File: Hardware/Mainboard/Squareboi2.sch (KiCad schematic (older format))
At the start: 25 parts, among them J1 GB-CART, J10 TP_CLK, J11 TP_40, J2 ROMC_L, J4 ROMC_C, J5 RAMC_L, J6 RAMC_R, J7 JTAG, J8 AUX_POW, SW1 SW_DIP_x02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

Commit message: Refactor pullup resistors
Add pullup to reset line for DMG compatibility, remove TDI and TMS pullups. Update mainboard to V2.02.
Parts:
- removed R6, R7: 20K, Resistor_THT:R_Axial_DIN0207_L6.3mm_D2.5mm_P10.16mm_Horizontal, symbol Device:R
- added J12: TP_RST, Connector_PinSocket_2.54mm:PinSocket_1x01_P2.54mm_Vertical, symbol Connector_Generic:Conn_01x01
- added R10: 100K, Resistor_THT:R_Axial_DIN0207_L6.3mm_D2.5mm_P10.16mm_Horizontal, symbol Device:R
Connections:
- wire segments 262 -> 260
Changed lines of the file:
@@
 	-1   0    0    1
 $EndComp
-Connection ~ 13150 8700
-Wire Wire Line
-	13300 8700 13300 8800
-Wire Wire Line
-	13150 8700 13300 8700
-Wire Wire Line
-	12950 8700 13150 8700
-Wire Wire Line
-	12950 8800 12950 8700
-$Comp
-L power:+5V #PWR0102
-U 1 1 61C3EE7B
-P 13150 8700
-F 0 "#PWR0102" H 13150 8550 50  0001 C CNN
-F 1 "+5V" H 13165 8873 50  0000 C CNN
-F 2 "" H 13150 8700 50  0001 C CNN
-F 3 "" H 13150 8700 50  0001 C CNN
-	1    13150 8700
-	1    0    0    -1
-$EndComp
 Wire Wire Line
 	12950 9350 12950 9550
-Connection ~ 12950 9350
 Wire Wire Line
 	12950 9350 12900 9350
-Connection ~ 13300 9350
-Wire Wire Line
-	13300 9350 13250 9350
-Wire Wire Line
-	12950 9100 12950 9350
-Wire Wire Line
-	13300 9100 13300 9350
-$Comp
-L Device:R R6
-U 1 1 61B8CCC5
-P 12950 8950
-F 0 "R6" H 13020 8996 50  0000 L CNN
-F 1 "20K" H 13020 8905 50  0000 L CNN
-F 2 "Resistor_THT:R_Axial_DIN0207_L6.3mm_D2.5mm_P10.16mm_Horizontal" V 12880 8950 50  0001 C CNN
-F 3 "~" H 12950 8950 50  0001 C CNN
-	1    12950 8950
-	1    0    0    -1
-$EndComp
-$Comp
-L Device:R R7
-U 1 1 61B8C6E8
-P 13300 8950
-F 0 "R7" H 13230 8904 50  0000 R CNN
-F 1 "20K" H 13230 8995 50  0000 R CNN
-F 2 "Resistor_THT:R_Axial_DIN0207_L6.3mm_D2.5mm_P10.16mm_Horizontal" V 13230 8950 50  0001 C CNN
-F 3 "~" H 13300 8950 50  0001 C CNN
-	1    13300 8950
-	-1   0    0    1
-$EndComp
 Text Label 12900 9350 2    50   ~ 0
 TDI
@@
 	13650 9150 14300 9150
 Connection ~ 13650 9150
-Wire Wire Line
-	13300 9350 14300 9350
 Wire Wire Line
 	12950 9550 14300 9550
@@
 	1300 6350 1650 6350
 $Comp
-L power:GND #PWR?
+L power:GND #PWR0101
 U 1 1 629EA1B7
 P 7150 6250
-F 0 "#PWR?" H 7150 6000 50  0001 C CNN
+F 0 "#PWR0101" H 7150 6000 50  0001 C CNN
 F 1 "GND" H 7155 6077 50  0000 C CNN
 F 2 "" H 7150 6250 50  0001 C CNN
@@
 Text Label 6950 6550 2    50   ~ 0
 IO40
+$Comp
+L Device:R R10
+U 1 1 6305FCD5
+P 14900 5850
+F 0 "R10" H 14970 5896 50  0000 L CNN
+F 1 "100K" H 14970 5805 50  0000 L CNN
+F 2 "Resistor_THT:R_Axial_DIN0207_L6.3mm_D2.5mm_P10.16mm_Horizontal" V 14830 5850 50  0001 C CNN
+F 3 "~" H 14900 5850 50  0001 C CNN
+	1    14900 5850
+	1    0    0    -1
+$EndComp
+Wire Wire Line
+	14900 5700 14900 5650
+Wire Wire Line
+	14900 5650 14550 5650
+Connection ~ 14550 5650
+Wire Wire Line
+	14900 6000 14900 6650
+Wire Wire Line
+	14900 6650 13500 6650
+Text Label 13500 6650 0    50   ~ 0
+RS_N
+$Comp
+L Connector_Generic:Conn_01x01 J12
+U 1 1 63093FFD
+P 1850 5850
+F 0 "J12" H 1930 5842 50  0000 L CNN
+F 1 "TP_RST" H 1930 5751 50  0000 L CNN
+F 2 "Connector_PinSocket_2.54mm:PinSocket_1x01_P2.54mm_Vertical" H 1850 5850 50  0001 C CNN
+F 3 "~" H 1850 5850 50  0001 C CNN
+	1    1850 5850
+	1    0    0    -1
+$EndComp
+Text Label 1300 5850 0    50   ~ 0
+RS_N
+Wire Wire Line
+	1300 5850 1650 5850
+Wire Wire Line
+	13250 9350 14300 9350
 $EndSCHEMATC

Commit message: Remove reset pullup from Mainboard
Remove the RS_N pullup resistor after fixing pin keeper issue in software. Repackage corresponding gerbers.
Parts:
- removed R10: 100K, Resistor_THT:R_Axial_DIN0207_L6.3mm_D2.5mm_P10.16mm_Horizontal, symbol Device:R
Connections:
- wire segments 260 -> 254
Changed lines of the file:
@@
 	1    0    0    -1
 $EndComp
-Text Label 14150 9250 2    50   ~ 0
+Text Label 14000 9250 0    50   ~ 0
 TDO
-Wire Wire Line
-	14300 9250 14150 9250
 $Comp
 L power:+5V #PWR09
@@
 	-1   0    0    1
 $EndComp
-Wire Wire Line
-	12950 9350 12950 9550
-Wire Wire Line
-	12950 9350 12900 9350
-Text Label 12900 9350 2    50   ~ 0
+Text Label 14000 9550 0    50   ~ 0
 TDI
-Text Label 13250 9350 2    50   ~ 0
+Text Label 14000 9350 0    50   ~ 0
 TMS
 Text Label 13600 9150 2    50   ~ 0
@@
 	13650 9150 14300 9150
 Connection ~ 13650 9150
-Wire Wire Line
-	12950 9550 14300 9550
 $Comp
 L power:GND #PWR0103
@@
 IO40
 $Comp
-L Device:R R10
-U 1 1 6305FCD5
-P 14900 5850
-F 0 "R10" H 14970 5896 50  0000 L CNN
-F 1 "100K" H 14970 5805 50  0000 L CNN
-F 2 "Resistor_THT:R_Axial_DIN0207_L6.3mm_D2.5mm_P10.16mm_Horizontal" V 14830 5850 50  0001 C CNN
-F 3 "~" H 14900 5850 50  0001 C CNN
-	1    14900 5850
-	1    0    0    -1
-$EndComp
-Wire Wire Line
-	14900 5700 14900 5650
-Wire Wire Line
-	14900 5650 14550 5650
-Connection ~ 14550 5650
-Wire Wire Line
-	14900 6000 14900 6650
-Wire Wire Line
-	14900 6650 13500 6650
-Text Label 13500 6650 0    50   ~ 0
-RS_N
-$Comp
 L Connector_Generic:Conn_01x01 J12
 U 1 1 63093FFD
@@
 	1300 5850 1650 5850
 Wire Wire Line
-	13250 9350 14300 9350
+	14000 9250 14300 9250
+Wire Wire Line
+	14300 9350 14000 9350
+Wire Wire Line
+	14300 9550 14000 9550
 $EndSCHEMATC

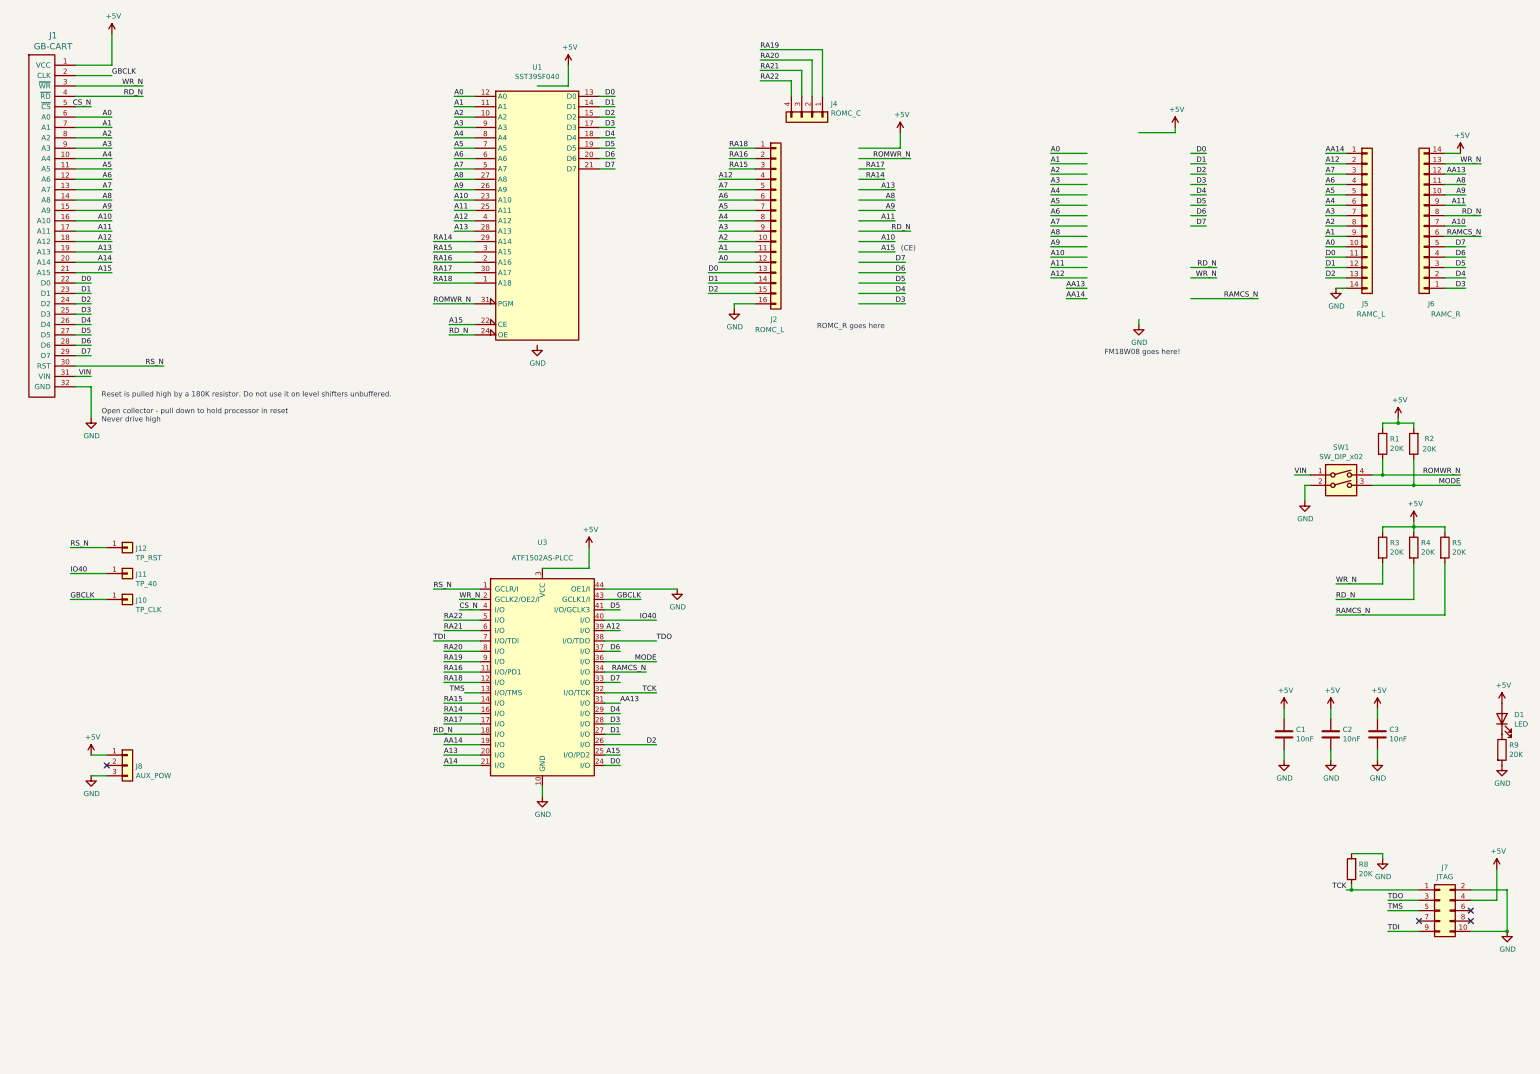
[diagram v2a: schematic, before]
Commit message: Update schematic capacitors
Move capacitor symbols to be closer to devices they're decoupling, fix value typo (10nf to 100nf)
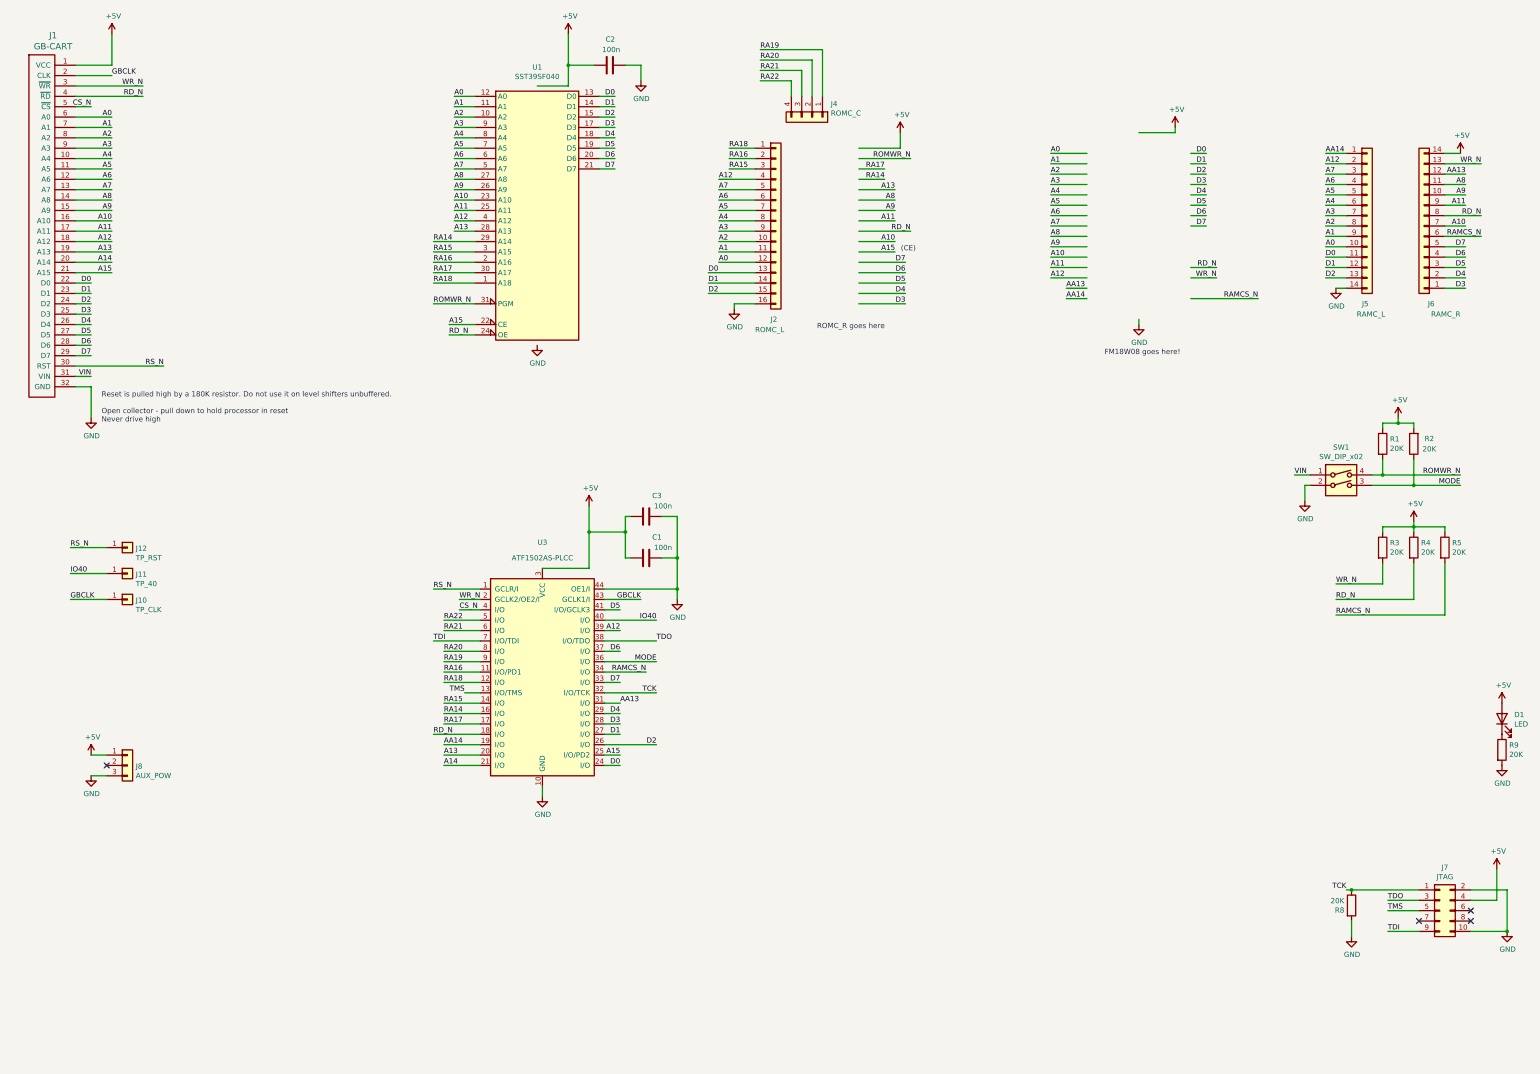
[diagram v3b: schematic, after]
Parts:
- C1, C2, C3: value 10nF -> 100n
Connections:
- wire segments 254 -> 261
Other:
- moved on the sheet: C1, C2, C3, R8
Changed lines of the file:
@@
 L Device:C C1
 U 1 1 619552DE
-P 13000 7650
-F 0 "C1" H 13115 7696 50  0000 L CNN
-F 1 "10nF" H 13115 7605 50  0000 L CNN
-F 2 "Capacitor_THT:CP_Radial_D5.0mm_P2.50mm" H 13038 7500 50  0001 C CNN
-F 3 "~" H 13000 7650 50  0001 C CNN
-	1    13000 7650
-	1    0    0    -1
+P 6850 5950
+F 0 "C1" V 7050 5800 50  0000 L CNN
+F 1 "100n" V 6950 5700 50  0000 L CNN
+F 2 "Capacitor_THT:CP_Radial_D5.0mm_P2.50mm" H 6888 5800 50  0001 C CNN
+F 3 "~" H 6850 5950 50  0001 C CNN
+	1    6850 5950
+	0    -1   -1   0
 $EndComp
 $Comp
 L Device:C C2
 U 1 1 6195603A
-P 13450 7650
-F 0 "C2" H 13565 7696 50  0000 L CNN
-F 1 "10nF" H 13565 7605 50  0000 L CNN
-F 2 "Capacitor_THT:CP_Radial_D5.0mm_P2.50mm" H 13488 7500 50  0001 C CNN
-F 3 "~" H 13450 7650 50  0001 C CNN
-	1    13450 7650
-	1    0    0    -1
-$EndComp
-$Comp
-L power:+5V #PWR016
-U 1 1 61956E01
-P 13000 7400
-F 0 "#PWR016" H 13000 7250 50  0001 C CNN
-F 1 "+5V" H 13015 7573 50  0000 C CNN
-F 2 "" H 13000 7400 50  0001 C CNN
-F 3 "" H 13000 7400 50  0001 C CNN
-	1    13000 7400
-	1    0    0    -1
-$EndComp
-$Comp
-L power:+5V #PWR018
-U 1 1 61957A03
-P 13450 7400
-F 0 "#PWR018" H 13450 7250 50  0001 C CNN
-F 1 "+5V" H 13465 7573 50  0000 C CNN
-F 2 "" H 13450 7400 50  0001 C CNN
-F 3 "" H 13450 7400 50  0001 C CNN
-	1    13450 7400
-	1    0    0    -1
-$EndComp
-$Comp
-L power:GND #PWR017
-U 1 1 619586BC
-P 13000 7900
-F 0 "#PWR017" H 13000 7650 50  0001 C CNN
-F 1 "GND" H 13005 7727 50  0000 C CNN
-F 2 "" H 13000 7900 50  0001 C CNN
-F 3 "" H 13000 7900 50  0001 C CNN
-	1    13000 7900
-	1    0    0    -1
+P 6500 1200
+F 0 "C2" V 6750 1150 50  0000 L CNN
+F 1 "100n" V 6650 1100 50  0000 L CNN
+F 2 "Capacitor_THT:CP_Radial_D5.0mm_P2.50mm" H 6538 1050 50  0001 C CNN
+F 3 "~" H 6500 1200 50  0001 C CNN
+	1    6500 1200
+	0    -1   -1   0
 $EndComp
 $Comp
 L power:GND #PWR019
 U 1 1 6195988B
-P 13450 7900
-F 0 "#PWR019" H 13450 7650 50  0001 C CNN
-F 1 "GND" H 13455 7727 50  0000 C CNN
-F 2 "" H 13450 7900 50  0001 C CNN
-F 3 "" H 13450 7900 50  0001 C CNN
-	1    13450 7900
-	1    0    0    -1
-$EndComp
-Wire Wire Line
-	13000 7900 13000 7800
-Wire Wire Line
-	13450 7900 13450 7800
-Wire Wire Line
-	13450 7500 13450 7400
-Wire Wire Line
-	13000 7500 13000 7400
+P 6800 1350
+F 0 "#PWR019" H 6800 1100 50  0001 C CNN
+F 1 "GND" H 6805 1177 50  0000 C CNN
+F 2 "" H 6800 1350 50  0001 C CNN
+F 3 "" H 6800 1350 50  0001 C CNN
+	1    6800 1350
+	1    0    0    -1
+$EndComp
 Text Label 2000 1400 2    50   ~ 0
 WR_N
@@
 Wire Wire Line
 	5800 1400 6100 1400
-Wire Wire Line
-	6100 1400 6100 1200
 $Comp
 L power:+5V #PWR012
 U 1 1 6195E0A3
-P 6100 1200
-F 0 "#PWR012" H 6100 1050 50  0001 C CNN
-F 1 "+5V" H 6115 1373 50  0000 C CNN
-F 2 "" H 6100 1200 50  0001 C CNN
-F 3 "" H 6100 1200 50  0001 C CNN
-	1    6100 1200
+P 6100 900
+F 0 "#PWR012" H 6100 750 50  0001 C CNN
+F 1 "+5V" H 6115 1073 50  0000 C CNN
+F 2 "" H 6100 900 50  0001 C CNN
+F 3 "" H 6100 900 50  0001 C CNN
+	1    6100 900
 	1    0    0    -1
 $EndComp
@@
 L power:+5V #PWR025
 U 1 1 61A9380D
-P 6300 5850
-F 0 "#PWR025" H 6300 5700 50  0001 C CNN
-F 1 "+5V" H 6315 6023 50  0000 C CNN
-F 2 "" H 6300 5850 50  0001 C CNN
-F 3 "" H 6300 5850 50  0001 C CNN
-	1    6300 5850
+P 6300 5450
+F 0 "#PWR025" H 6300 5300 50  0001 C CNN
+F 1 "+5V" H 6315 5623 50  0000 C CNN
+F 2 "" H 6300 5450 50  0001 C CNN
+F 3 "" H 6300 5450 50  0001 C CNN
+	1    6300 5450
 	1    0    0    -1
 $EndComp
 Wire Wire Line
 	5850 6050 6300 6050
-Wire Wire Line
-	6300 6050 6300 5850
 $Comp
 L power:GND #PWR022
@@
 L Device:R R8
 U 1 1 61BA0B3B
-P 13650 8950
-F 0 "R8" H 13580 8904 50  0000 R CNN
-F 1 "20K" H 13580 8995 50  0000 R CNN
-F 2 "Resistor_THT:R_Axial_DIN0207_L6.3mm_D2.5mm_P10.16mm_Horizontal" V 13580 8950 50  0001 C CNN
-F 3 "~" H 13650 8950 50  0001 C CNN
-	1    13650 8950
-	-1   0    0    1
+P 13650 9300
+F 0 "R8" H 13580 9254 50  0000 R CNN
+F 1 "20K" H 13580 9345 50  0000 R CNN
+F 2 "Resistor_THT:R_Axial_DIN0207_L6.3mm_D2.5mm_P10.16mm_Horizontal" V 13580 9300 50  0001 C CNN
+F 3 "~" H 13650 9300 50  0001 C CNN
+	1    13650 9300
+	1    0    0    -1
 $EndComp
 Text Label 14000 9550 0    50   ~ 0
@@
 TCK
 Wire Wire Line
-	13650 9100 13650 9150
-Wire Wire Line
 	13650 9150 13600 9150
 Wire Wire Line
@@
 L power:GND #PWR0103
 U 1 1 61CF9782
-P 13950 8850
-F 0 "#PWR0103" H 13950 8600 50  0001 C CNN
-F 1 "GND" H 13955 8677 50  0000 C CNN
-F 2 "" H 13950 8850 50  0001 C CNN
-F 3 "" H 13950 8850 50  0001 C CNN
-	1    13950 8850
-	1    0    0    -1
-$EndComp
-Wire Wire Line
-	13950 8800 13950 8850
-Wire Wire Line
-	13650 8800 13950 8800
+P 13650 9600
+F 0 "#PWR0103" H 13650 9350 50  0001 C CNN
+F 1 "GND" H 13655 9427 50  0000 C CNN
+F 2 "" H 13650 9600 50  0001 C CNN
+F 3 "" H 13650 9600 50  0001 C CNN
+	1    13650 9600
+	1    0    0    -1
+$EndComp
 $Comp
 L power:GND #PWR020
@@
 L Device:C C3
 U 1 1 61DD3167
-P 13900 7650
-F 0 "C3" H 14015 7696 50  0000 L CNN
-F 1 "10nF" H 14015 7605 50  0000 L CNN
-F 2 "Capacitor_THT:CP_Radial_D5.0mm_P2.50mm" H 13938 7500 50  0001 C CNN
-F 3 "~" H 13900 7650 50  0001 C CNN
-	1    13900 7650
-	1    0    0    -1
-$EndComp
-$Comp
-L power:+5V #PWR0104
-U 1 1 61DD360F
-P 13900 7400
-F 0 "#PWR0104" H 13900 7250 50  0001 C CNN
-F 1 "+5V" H 13915 7573 50  0000 C CNN
-F 2 "" H 13900 7400 50  0001 C CNN
-F 3 "" H 13900 7400 50  0001 C CNN
-	1    13900 7400
-	1    0    0    -1
-$EndComp
-$Comp
-L power:GND #PWR0105
-U 1 1 61DD3619
-P 13900 7900
-F 0 "#PWR0105" H 13900 7650 50  0001 C CNN
-F 1 "GND" H 13905 7727 50  0000 C CNN
-F 2 "" H 13900 7900 50  0001 C CNN
-F 3 "" H 13900 7900 50  0001 C CNN
-	1    13900 7900
-	1    0    0    -1
-$EndComp
-Wire Wire Line
-	13900 7800 13900 7900
-Wire Wire Line
-	13900 7500 13900 7400
+P 6850 5550
+F 0 "C3" V 7050 5400 50  0000 L CNN
+F 1 "100n" V 6950 5300 50  0000 L CNN
+F 2 "Capacitor_THT:CP_Radial_D5.0mm_P2.50mm" H 6888 5400 50  0001 C CNN
+F 3 "~" H 6850 5550 50  0001 C CNN
+	1    6850 5550
+	0    -1   -1   0
+$EndComp
 $Comp
 L Connector_Generic:Conn_01x01 J10
@@
 L power:GND #PWR0101
 U 1 1 629EA1B7
-P 7150 6250
-F 0 "#PWR0101" H 7150 6000 50  0001 C CNN
-F 1 "GND" H 7155 6077 50  0000 C CNN
-F 2 "" H 7150 6250 50  0001 C CNN
-F 3 "" H 7150 6250 50  0001 C CNN
-	1    7150 6250
+P 7150 6350
+F 0 "#PWR0101" H 7150 6100 50  0001 C CNN
+F 1 "GND" H 7155 6177 50  0000 C CNN
+F 2 "" H 7150 6350 50  0001 C CNN
+F 3 "" H 7150 6350 50  0001 C CNN
+	1    7150 6350
 	1    0    0    -1
 $EndComp
@@
 Wire Wire Line
 	14300 9550 14000 9550
+Wire Wire Line
+	6100 900  6100 1200
+Connection ~ 6100 1200
+Wire Wire Line
+	6100 1200 6100 1400
+Wire Wire Line
+	6800 1200 6800 1350
+Wire Wire Line
+	6650 1200 6800 1200
+Wire Wire Line
+	6100 1200 6350 1200
+Wire Wire Line
+	6300 5700 6650 5700
+Wire Wire Line
+	6650 5700 6650 5550
+Wire Wire Line
+	6650 5550 6700 5550
+Wire Wire Line
+	6300 5700 6300 6050
+Wire Wire Line
+	6650 5700 6650 5950
+Wire Wire Line
+	6650 5950 6700 5950
+Connection ~ 6650 5700
+Wire Wire Line
+	6300 5450 6300 5700
+Connection ~ 6300 5700
+Wire Wire Line
+	7000 5550 7150 5550
+Wire Wire Line
+	7150 5550 7150 5950
+Connection ~ 7150 6250
+Wire Wire Line
+	7000 5950 7150 5950
+Connection ~ 7150 5950
+Wire Wire Line
+	7150 5950 7150 6250
+Wire Wire Line
+	7150 6250 7150 6350
+Wire Wire Line
+	13650 9450 13650 9600
 $EndSCHEMATC
